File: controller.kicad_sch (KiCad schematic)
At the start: 40 parts, among them U3 STM32F767ZITx, Y1 25MHz

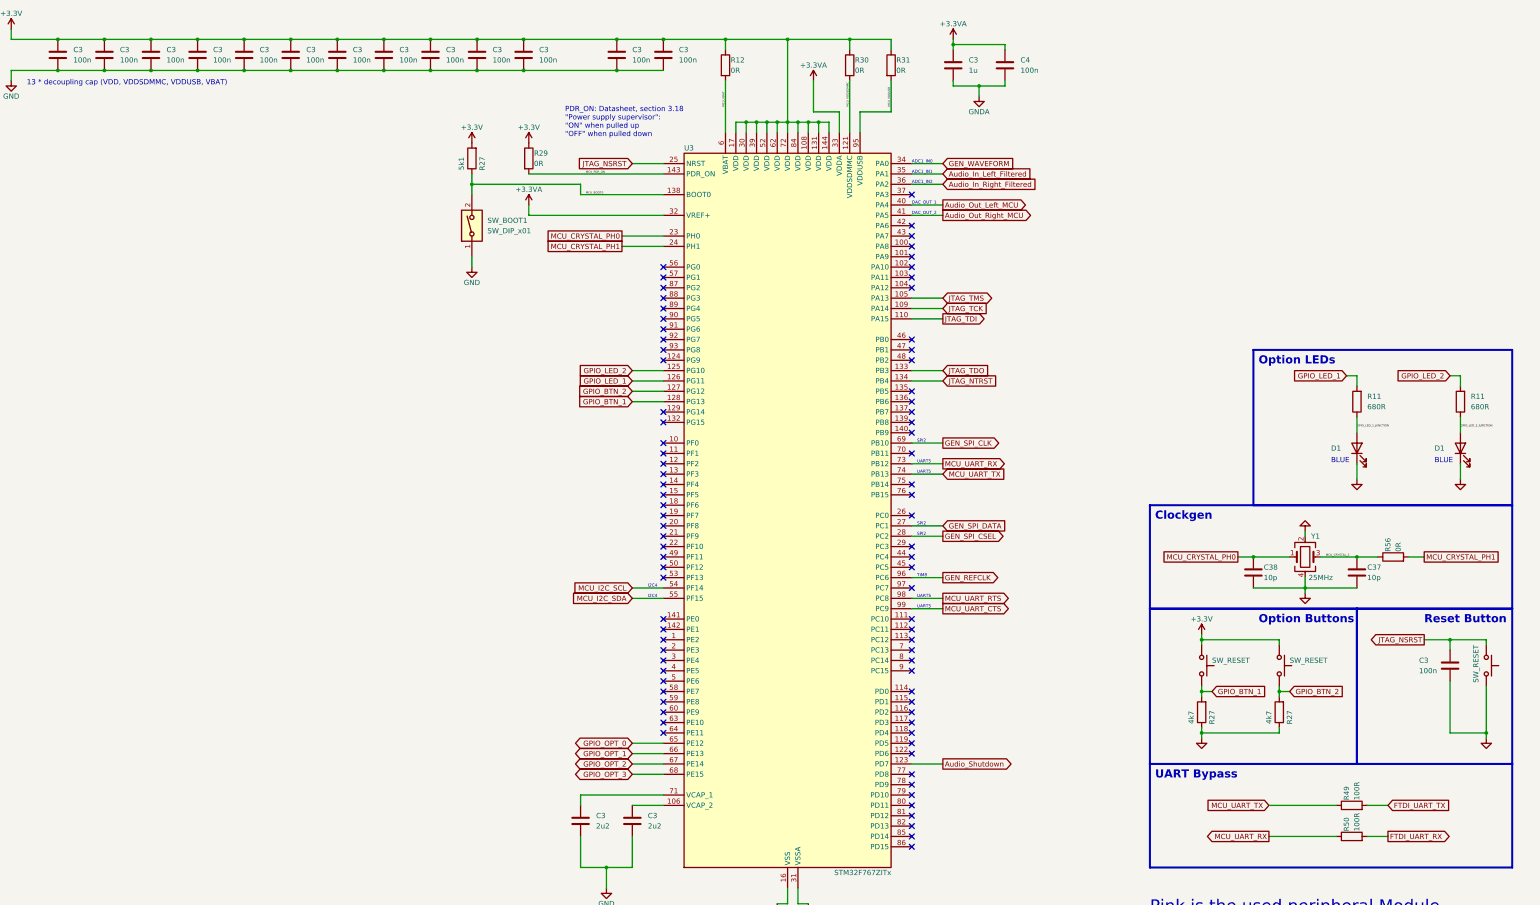
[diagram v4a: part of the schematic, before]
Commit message: Added capacitor voltage rating
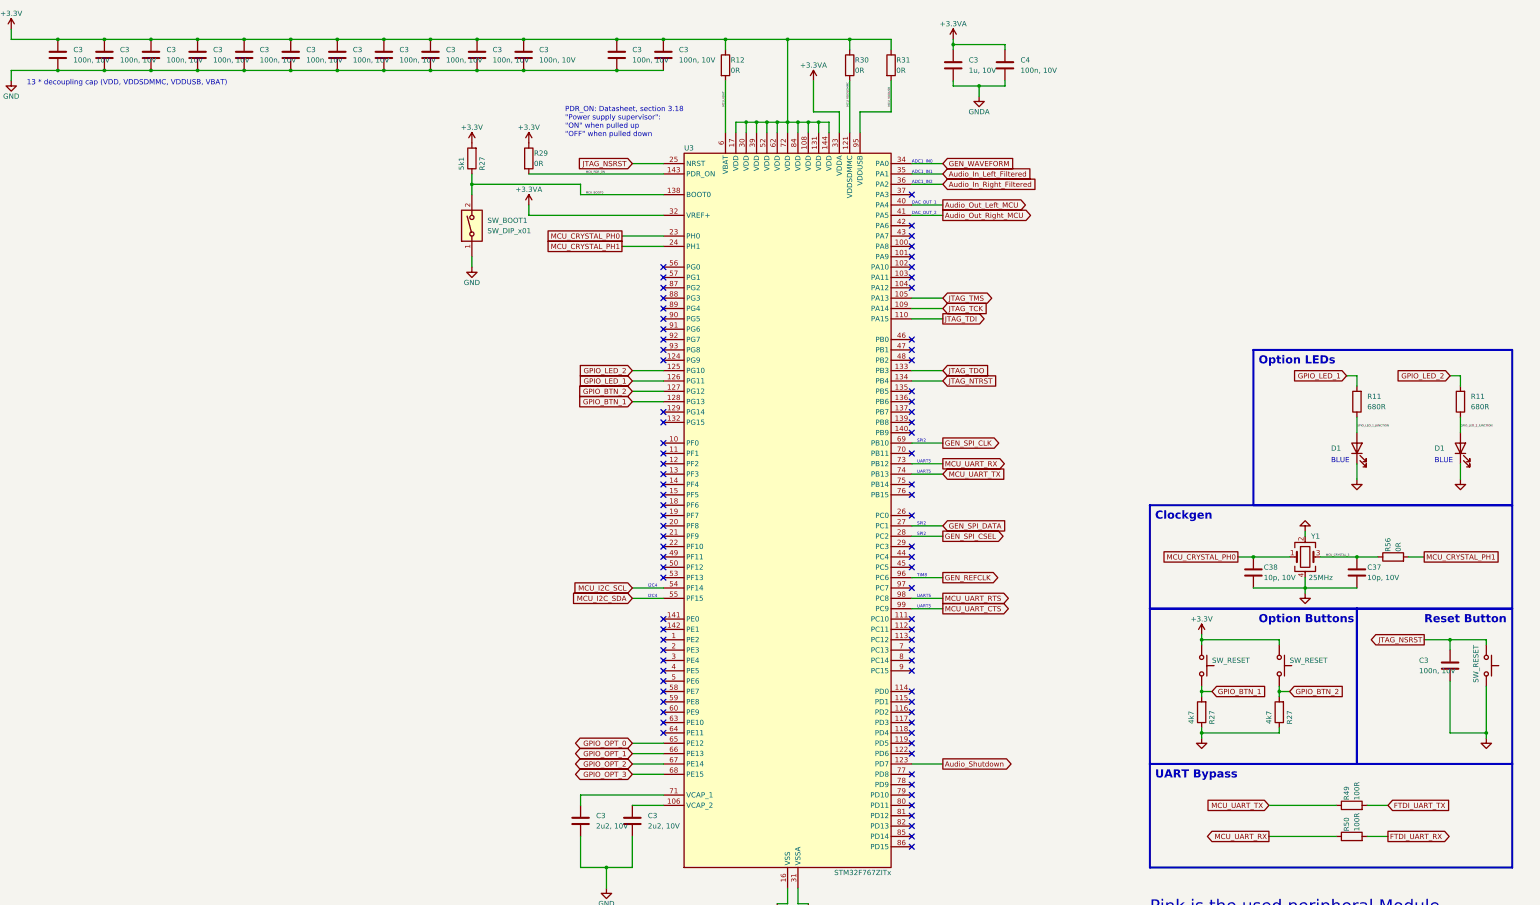
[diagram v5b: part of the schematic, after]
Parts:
- C3: value 2u2 -> 2u2, 10V
- C3, C4: value 100n -> 100n, 10V
- C3: value 1u -> 1u, 10V
- C37, C38: value 10p -> 10p, 10V
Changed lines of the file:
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@@
       (effects (font (size 1.27 1.27)) (justify left))
     )
-    (property "Value" "2u2" (at 181.61 231.14 0)
+    (property "Value" "2u2, 10V" (at 181.61 231.14 0)
       (effects (font (size 1.27 1.27)) (justify left))
     )
@@
       (effects (font (size 1.27 1.27)) (justify left))
     )
-    (property "Value" "100n" (at 177.8 43.18 0)
+    (property "Value" "100n, 10V" (at 177.8 43.18 0)
       (effects (font (size 1.27 1.27)) (justify left))
     )
@@
       (effects (font (size 1.27 1.27)) (justify left))
     )
-    (property "Value" "100n" (at 63.5 43.18 0)
+    (property "Value" "100n, 10V" (at 63.5 43.18 0)
       (effects (font (size 1.27 1.27)) (justify left))
     )
@@
       (effects (font (size 1.27 1.27)) (justify left))
     )
-    (property "Value" "100n" (at 143.51 43.18 0)
+    (property "Value" "100n, 10V" (at 143.51 43.18 0)
       (effects (font (size 1.27 1.27)) (justify left))
     )
@@
       (effects (font (size 1.27 1.27)) (justify left))
     )
-    (property "Value" "10p" (at 358.14 170.18 0)
+    (property "Value" "10p, 10V" (at 358.14 170.18 0)
       (effects (font (size 1.27 1.27)) (justify left))
     )
@@
       (effects (font (size 1.27 1.27)) (justify left))
     )
-    (property "Value" "100n" (at 52.07 43.18 0)
+    (property "Value" "100n, 10V" (at 52.07 43.18 0)
       (effects (font (size 1.27 1.27)) (justify left))
     )
@@
       (effects (font (size 1.27 1.27)) (justify left))
     )
-    (property "Value" "100n" (at 86.36 43.18 0)
+    (property "Value" "100n, 10V" (at 86.36 43.18 0)
       (effects (font (size 1.27 1.27)) (justify left))
     )
@@
       (effects (font (size 1.27 1.27)) (justify left))
     )
-    (property "Value" "100n" (at 97.79 43.18 0)
+    (property "Value" "100n, 10V" (at 97.79 43.18 0)
       (effects (font (size 1.27 1.27)) (justify left))
     )
@@
       (effects (font (size 1.27 1.27)) (justify left))
     )
-    (property "Value" "1u" (at 260.35 45.72 0)
+    (property "Value" "1u, 10V" (at 260.35 45.72 0)
       (effects (font (size 1.27 1.27)) (justify left))
     )
@@
       (effects (font (size 1.27 1.27)) (justify left))
     )
-    (property "Value" "100n" (at 273.05 45.72 0)
+    (property "Value" "100n, 10V" (at 273.05 45.72 0)
       (effects (font (size 1.27 1.27)) (justify left))
     )
@@
       (effects (font (size 1.27 1.27)) (justify left))
     )
-    (property "Value" "100n" (at 40.64 43.18 0)
+    (property "Value" "100n, 10V" (at 40.64 43.18 0)
       (effects (font (size 1.27 1.27)) (justify left))
     )
@@
       (effects (font (size 1.27 1.27)) (justify left))
     )
-    (property "Value" "100n" (at 120.65 43.18 0)
+    (property "Value" "100n, 10V" (at 120.65 43.18 0)
       (effects (font (size 1.27 1.27)) (justify left))
     )
@@
       (effects (font (size 1.27 1.27)) (justify left))
     )
-    (property "Value" "2u2" (at 168.91 231.14 0)
+    (property "Value" "2u2, 10V" (at 168.91 231.14 0)
       (effects (font (size 1.27 1.27)) (justify left))
     )
@@
       (effects (font (size 1.27 1.27)) (justify left))
     )
-    (property "Value" "100n" (at 370.84 193.04 0)
+    (property "Value" "100n, 10V" (at 370.84 193.04 0)
       (effects (font (size 1.27 1.27)) (justify left))
     )
@@
       (effects (font (size 1.27 1.27)) (justify left))
     )
-    (property "Value" "100n" (at 132.08 43.18 0)
+    (property "Value" "100n, 10V" (at 132.08 43.18 0)
       (effects (font (size 1.27 1.27)) (justify left))
     )
@@
       (effects (font (size 1.27 1.27)) (justify left))
     )
-    (property "Value" "100n" (at 74.93 43.18 0)
+    (property "Value" "100n, 10V" (at 74.93 43.18 0)
       (effects (font (size 1.27 1.27)) (justify left))
     )
@@
       (effects (font (size 1.27 1.27)) (justify left))
     )
-    (property "Value" "100n" (at 109.22 43.18 0)
+    (property "Value" "100n, 10V" (at 109.22 43.18 0)
       (effects (font (size 1.27 1.27)) (justify left))
     )
@@
       (effects (font (size 1.27 1.27)) (justify left))
     )
-    (property "Value" "10p" (at 332.74 170.18 0)
+    (property "Value" "10p, 10V" (at 332.74 170.18 0)
       (effects (font (size 1.27 1.27)) (justify left))
     )
@@
       (effects (font (size 1.27 1.27)) (justify left))
     )
-    (property "Value" "100n" (at 189.23 43.18 0)
+    (property "Value" "100n, 10V" (at 189.23 43.18 0)
       (effects (font (size 1.27 1.27)) (justify left))
     )
@@
       (effects (font (size 1.27 1.27)) (justify left))
     )
-    (property "Value" "100n" (at 154.94 43.18 0)
-      (effects (font (size 1.27 1.27)) (justify left))
-    )
+    (property "Value" "100n, 10V" (at 154.94 43.18 0)
+      (effects (font (size 1.27 1.27)) (justify left))
+    )
